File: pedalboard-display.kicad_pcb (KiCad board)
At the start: 2 copper layers, 24 x 24 mm, 32 parts, among them J1 02x02

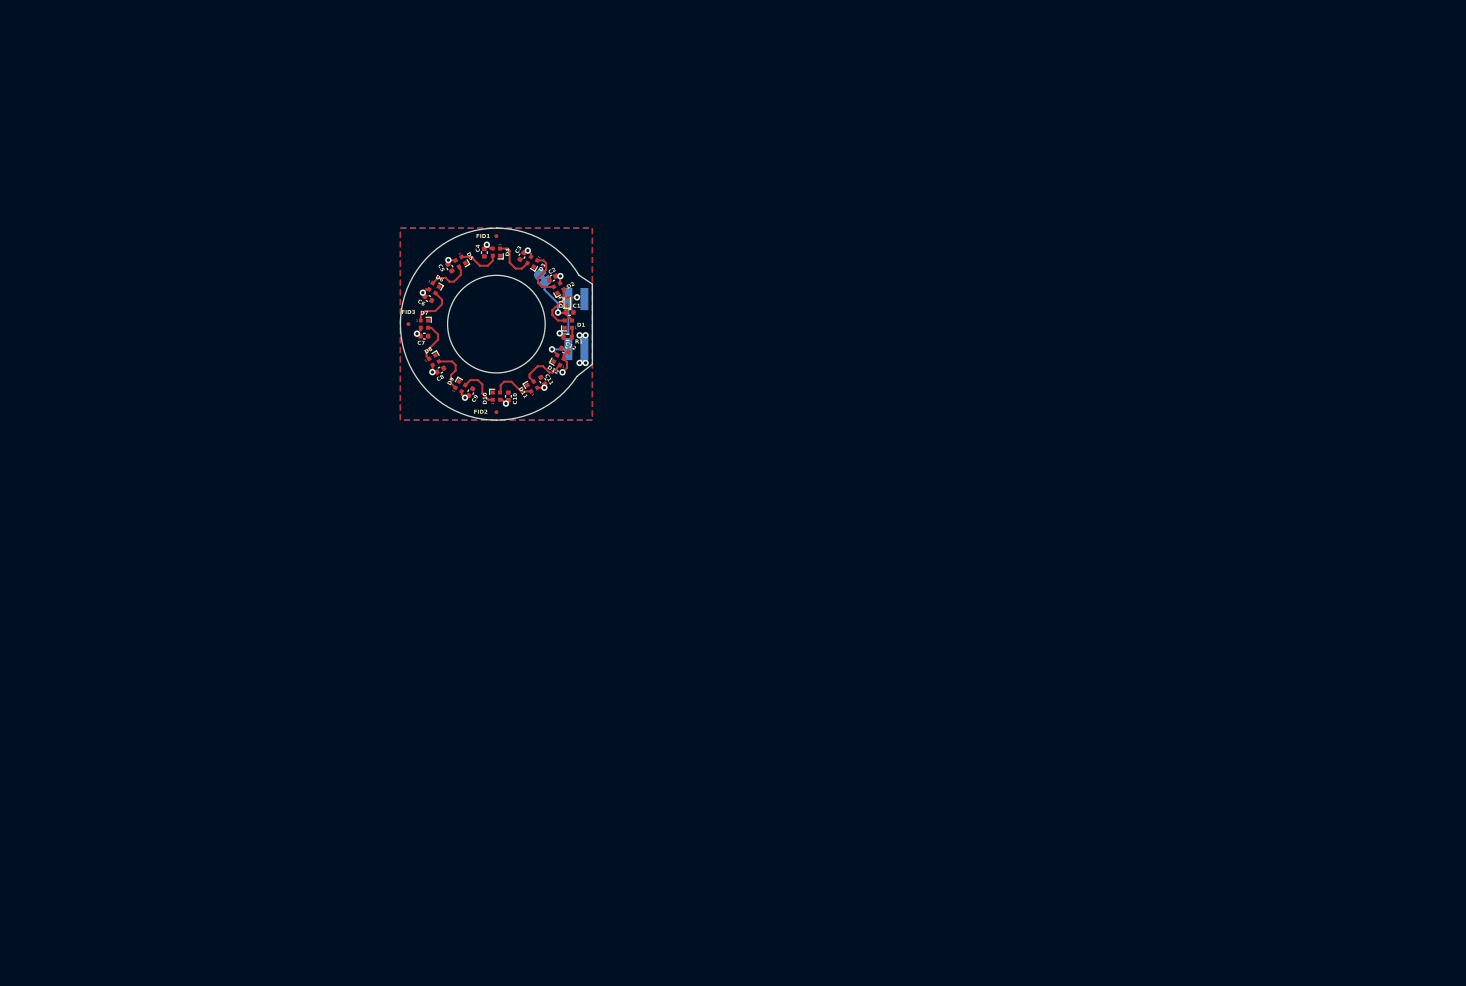
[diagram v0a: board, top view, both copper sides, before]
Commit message: First placement of parts on PCB
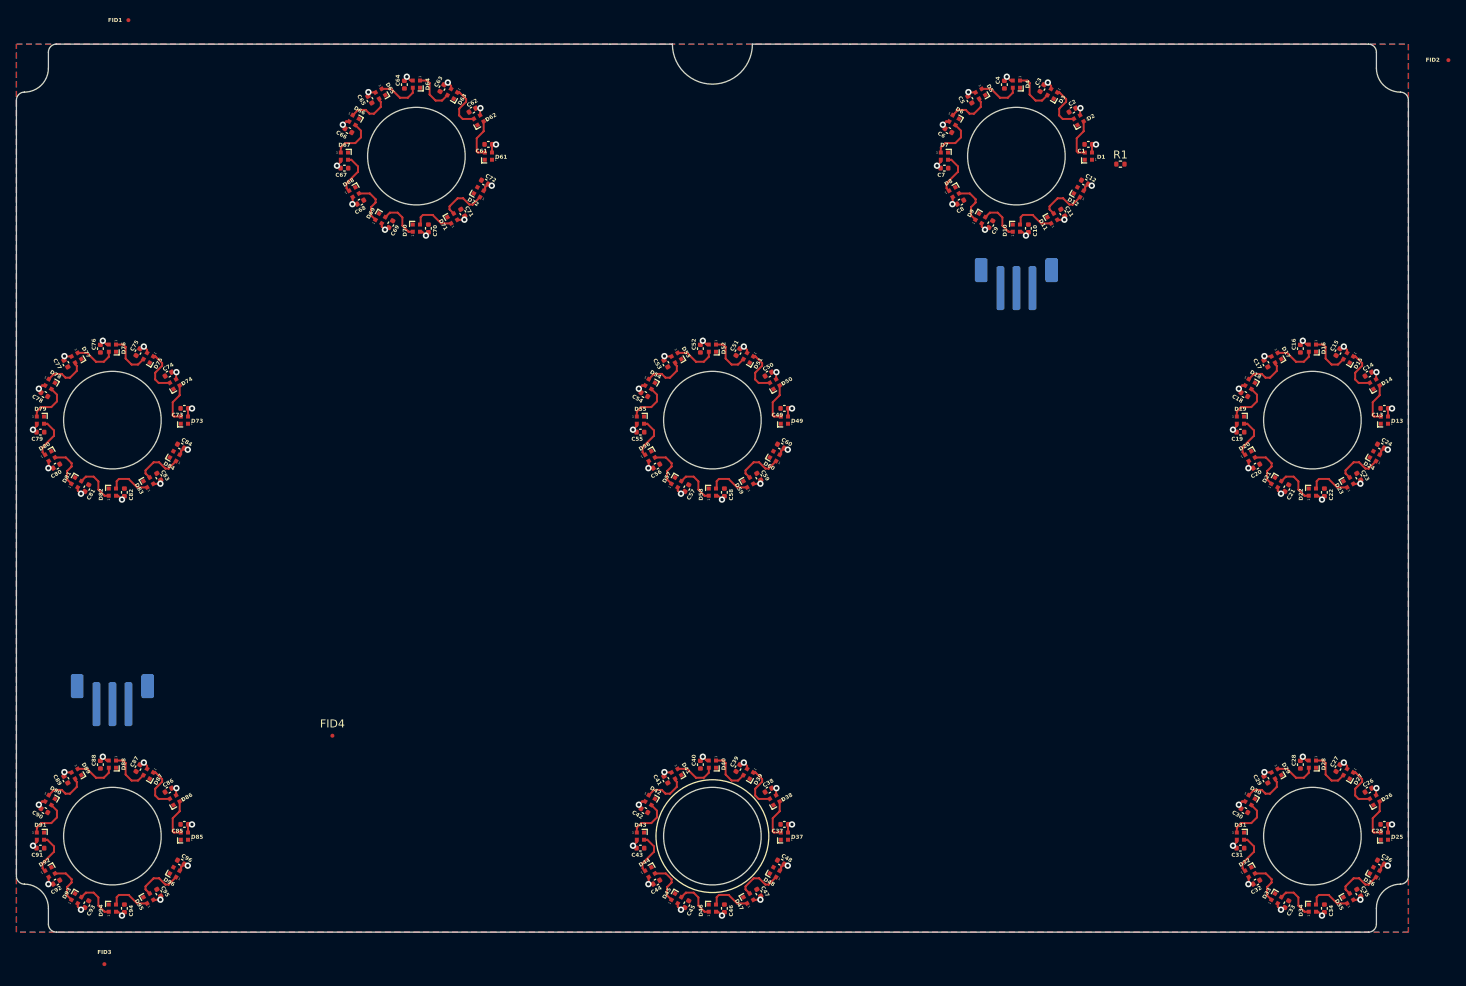
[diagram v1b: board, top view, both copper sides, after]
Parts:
- removed H4: Actuator Hole, Library:Actuator
- removed JP1: SJ, Jumper:SolderJumper-2_P1.3mm_Bridged_RoundedPad1.0x1.5mm
- added C13: 1uF, Capacitor_SMD:C_0402_1005Metric, F.Cu at (191.0, 70.5)
- added C14: 1uF, Capacitor_SMD:C_0402_1005Metric, F.Cu at (189.0, 66.2)
- added C15: 1uF, Capacitor_SMD:C_0402_1005Metric, F.Cu at (185.2, 63.5)
- added C16: 1uF, Capacitor_SMD:C_0402_1005Metric, F.Cu at (180.5, 63.1)
- added C17: 1uF, Capacitor_SMD:C_0402_1005Metric, F.Cu at (176.2, 64.9)
- added C18: 1uF, Capacitor_SMD:C_0402_1005Metric, F.Cu at (173.5, 68.8)
- added C19: 1uF, Capacitor_SMD:C_0402_1005Metric, F.Cu at (173.0, 73.5)
- added C20: 1uF, Capacitor_SMD:C_0402_1005Metric, F.Cu at (175.0, 77.8)
- added C21: 1uF, Capacitor_SMD:C_0402_1005Metric, F.Cu at (178.8, 80.5)
- added C22: 1uF, Capacitor_SMD:C_0402_1005Metric, F.Cu at (183.5, 81.0)
- added C23: 1uF, Capacitor_SMD:C_0402_1005Metric, F.Cu at (187.8, 79.1)
- added C24: 1uF, Capacitor_SMD:C_0402_1005Metric, F.Cu at (190.6, 75.2)
- added C25: 1uF, Capacitor_SMD:C_0402_1005Metric, F.Cu at (191.0, 122.5)
- added C26: 1uF, Capacitor_SMD:C_0402_1005Metric, F.Cu at (189.0, 118.2)
- added C27: 1uF, Capacitor_SMD:C_0402_1005Metric, F.Cu at (185.2, 115.5)
- added C28: 1uF, Capacitor_SMD:C_0402_1005Metric, F.Cu at (180.5, 115.1)
- added C29: 1uF, Capacitor_SMD:C_0402_1005Metric, F.Cu at (176.2, 116.9)
- added C30: 1uF, Capacitor_SMD:C_0402_1005Metric, F.Cu at (173.5, 120.8)
- added C31: 1uF, Capacitor_SMD:C_0402_1005Metric, F.Cu at (173.0, 125.5)
- added C32: 1uF, Capacitor_SMD:C_0402_1005Metric, F.Cu at (175.0, 129.8)
- added C33: 1uF, Capacitor_SMD:C_0402_1005Metric, F.Cu at (178.8, 132.5)
- added C34: 1uF, Capacitor_SMD:C_0402_1005Metric, F.Cu at (183.5, 133.0)
- added C35: 1uF, Capacitor_SMD:C_0402_1005Metric, F.Cu at (187.8, 131.1)
- added C36: 1uF, Capacitor_SMD:C_0402_1005Metric, F.Cu at (190.6, 127.2)
- added C37: 1uF, Capacitor_SMD:C_0402_1005Metric, F.Cu at (116.0, 122.5)
- added C38: 1uF, Capacitor_SMD:C_0402_1005Metric, F.Cu at (114.0, 118.2)
- added C39: 1uF, Capacitor_SMD:C_0402_1005Metric, F.Cu at (110.2, 115.5)
- added C40: 1uF, Capacitor_SMD:C_0402_1005Metric, F.Cu at (105.5, 115.1)
- added C41: 1uF, Capacitor_SMD:C_0402_1005Metric, F.Cu at (101.2, 116.9)
- added C42: 1uF, Capacitor_SMD:C_0402_1005Metric, F.Cu at (98.5, 120.8)
- added C43: 1uF, Capacitor_SMD:C_0402_1005Metric, F.Cu at (98.0, 125.5)
- added C44: 1uF, Capacitor_SMD:C_0402_1005Metric, F.Cu at (100.0, 129.8)
- added C45: 1uF, Capacitor_SMD:C_0402_1005Metric, F.Cu at (103.8, 132.5)
- added C46: 1uF, Capacitor_SMD:C_0402_1005Metric, F.Cu at (108.5, 133.0)
- added C47: 1uF, Capacitor_SMD:C_0402_1005Metric, F.Cu at (112.8, 131.1)
- added C48: 1uF, Capacitor_SMD:C_0402_1005Metric, F.Cu at (115.5, 127.2)
- added C49: 1uF, Capacitor_SMD:C_0402_1005Metric, F.Cu at (116.0, 70.5)
- added C50: 1uF, Capacitor_SMD:C_0402_1005Metric, F.Cu at (114.0, 66.2)
- added C51: 1uF, Capacitor_SMD:C_0402_1005Metric, F.Cu at (110.2, 63.5)
- added C52: 1uF, Capacitor_SMD:C_0402_1005Metric, F.Cu at (105.5, 63.1)
- added C53: 1uF, Capacitor_SMD:C_0402_1005Metric, F.Cu at (101.2, 64.9)
- added C54: 1uF, Capacitor_SMD:C_0402_1005Metric, F.Cu at (98.5, 68.8)
- added C55: 1uF, Capacitor_SMD:C_0402_1005Metric, F.Cu at (98.0, 73.5)
- added C56: 1uF, Capacitor_SMD:C_0402_1005Metric, F.Cu at (100.0, 77.8)
- added C57: 1uF, Capacitor_SMD:C_0402_1005Metric, F.Cu at (103.8, 80.5)
- added C58: 1uF, Capacitor_SMD:C_0402_1005Metric, F.Cu at (108.5, 81.0)
- added C59: 1uF, Capacitor_SMD:C_0402_1005Metric, F.Cu at (112.8, 79.1)
- added C60: 1uF, Capacitor_SMD:C_0402_1005Metric, F.Cu at (115.5, 75.2)
- added C61: 1uF, Capacitor_SMD:C_0402_1005Metric, F.Cu at (79.0, 37.5)
- added C62: 1uF, Capacitor_SMD:C_0402_1005Metric, F.Cu at (77.0, 33.2)
- added C63: 1uF, Capacitor_SMD:C_0402_1005Metric, F.Cu at (73.2, 30.5)
- added C64: 1uF, Capacitor_SMD:C_0402_1005Metric, F.Cu at (68.5, 30.1)
- added C65: 1uF, Capacitor_SMD:C_0402_1005Metric, F.Cu at (64.2, 31.9)
- added C66: 1uF, Capacitor_SMD:C_0402_1005Metric, F.Cu at (61.5, 35.8)
- added C67: 1uF, Capacitor_SMD:C_0402_1005Metric, F.Cu at (61.0, 40.5)
- added C68: 1uF, Capacitor_SMD:C_0402_1005Metric, F.Cu at (63.0, 44.8)
- added C69: 1uF, Capacitor_SMD:C_0402_1005Metric, F.Cu at (66.8, 47.5)
- added C70: 1uF, Capacitor_SMD:C_0402_1005Metric, F.Cu at (71.5, 48.0)
- added C71: 1uF, Capacitor_SMD:C_0402_1005Metric, F.Cu at (75.8, 46.1)
- added C72: 1uF, Capacitor_SMD:C_0402_1005Metric, F.Cu at (78.5, 42.2)
- added C73: 1uF, Capacitor_SMD:C_0402_1005Metric, F.Cu at (41.0, 70.5)
- added C74: 1uF, Capacitor_SMD:C_0402_1005Metric, F.Cu at (39.0, 66.2)
- added C75: 1uF, Capacitor_SMD:C_0402_1005Metric, F.Cu at (35.2, 63.5)
- added C76: 1uF, Capacitor_SMD:C_0402_1005Metric, F.Cu at (30.5, 63.1)
- added C77: 1uF, Capacitor_SMD:C_0402_1005Metric, F.Cu at (26.2, 64.9)
- added C78: 1uF, Capacitor_SMD:C_0402_1005Metric, F.Cu at (23.5, 68.8)
- added C79: 1uF, Capacitor_SMD:C_0402_1005Metric, F.Cu at (23.0, 73.5)
- added C80: 1uF, Capacitor_SMD:C_0402_1005Metric, F.Cu at (25.0, 77.8)
- added C81: 1uF, Capacitor_SMD:C_0402_1005Metric, F.Cu at (28.8, 80.5)
- added C82: 1uF, Capacitor_SMD:C_0402_1005Metric, F.Cu at (33.5, 81.0)
- added C83: 1uF, Capacitor_SMD:C_0402_1005Metric, F.Cu at (37.8, 79.1)
- added C84: 1uF, Capacitor_SMD:C_0402_1005Metric, F.Cu at (40.5, 75.2)
- added C85: 1uF, Capacitor_SMD:C_0402_1005Metric, F.Cu at (41.0, 122.5)
- added C86: 1uF, Capacitor_SMD:C_0402_1005Metric, F.Cu at (39.0, 118.2)
- added C87: 1uF, Capacitor_SMD:C_0402_1005Metric, F.Cu at (35.2, 115.5)
- added C88: 1uF, Capacitor_SMD:C_0402_1005Metric, F.Cu at (30.5, 115.1)
- added C89: 1uF, Capacitor_SMD:C_0402_1005Metric, F.Cu at (26.2, 116.9)
- added C90: 1uF, Capacitor_SMD:C_0402_1005Metric, F.Cu at (23.5, 120.8)
- added C91: 1uF, Capacitor_SMD:C_0402_1005Metric, F.Cu at (23.0, 125.5)
- added C92: 1uF, Capacitor_SMD:C_0402_1005Metric, F.Cu at (25.0, 129.8)
- added C93: 1uF, Capacitor_SMD:C_0402_1005Metric, F.Cu at (28.8, 132.5)
- added C94: 1uF, Capacitor_SMD:C_0402_1005Metric, F.Cu at (33.5, 133.0)
- added C95: 1uF, Capacitor_SMD:C_0402_1005Metric, F.Cu at (37.8, 131.1)
- added C96: 1uF, Capacitor_SMD:C_0402_1005Metric, F.Cu at (40.5, 127.2)
- added D14: SK6812_EC15, Library:LED_SK6812_EC15_1.5x1.5mm, F.Cu at (189.8, 67.5)
- added D15: SK6812_EC15, Library:LED_SK6812_EC15_1.5x1.5mm, F.Cu at (186.5, 64.2)
- added D16: SK6812_EC15, Library:LED_SK6812_EC15_1.5x1.5mm, F.Cu at (182.0, 63.0)
- added D17: SK6812_EC15, Library:LED_SK6812_EC15_1.5x1.5mm, F.Cu at (177.5, 64.2)
- added D18: SK6812_EC15, Library:LED_SK6812_EC15_1.5x1.5mm, F.Cu at (174.2, 67.5)
- added D19: SK6812_EC15, Library:LED_SK6812_EC15_1.5x1.5mm, F.Cu at (173.0, 72.0)
- added D20: SK6812_EC15, Library:LED_SK6812_EC15_1.5x1.5mm, F.Cu at (174.2, 76.5)
- added D21: SK6812_EC15, Library:LED_SK6812_EC15_1.5x1.5mm, F.Cu at (177.5, 79.8)
- added D22: SK6812_EC15, Library:LED_SK6812_EC15_1.5x1.5mm, F.Cu at (182.0, 81.0)
- added D23: SK6812_EC15, Library:LED_SK6812_EC15_1.5x1.5mm, F.Cu at (186.5, 79.8)
- added D24: SK6812_EC15, Library:LED_SK6812_EC15_1.5x1.5mm, F.Cu at (189.8, 76.5)
- added D25: SK6812_EC15, Library:LED_SK6812_EC15_1.5x1.5mm, F.Cu at (191.0, 124.0)
- added D26: SK6812_EC15, Library:LED_SK6812_EC15_1.5x1.5mm, F.Cu at (189.8, 119.5)
- added D27: SK6812_EC15, Library:LED_SK6812_EC15_1.5x1.5mm, F.Cu at (186.5, 116.2)
- added D28: SK6812_EC15, Library:LED_SK6812_EC15_1.5x1.5mm, F.Cu at (182.0, 115.0)
- added D29: SK6812_EC15, Library:LED_SK6812_EC15_1.5x1.5mm, F.Cu at (177.5, 116.2)
- added D30: SK6812_EC15, Library:LED_SK6812_EC15_1.5x1.5mm, F.Cu at (174.2, 119.5)
- added D31: SK6812_EC15, Library:LED_SK6812_EC15_1.5x1.5mm, F.Cu at (173.0, 124.0)
- added D32: SK6812_EC15, Library:LED_SK6812_EC15_1.5x1.5mm, F.Cu at (174.2, 128.5)
- added D33: SK6812_EC15, Library:LED_SK6812_EC15_1.5x1.5mm, F.Cu at (177.5, 131.8)
- added D34: SK6812_EC15, Library:LED_SK6812_EC15_1.5x1.5mm, F.Cu at (182.0, 133.0)
- added D35: SK6812_EC15, Library:LED_SK6812_EC15_1.5x1.5mm, F.Cu at (186.5, 131.8)
- added D36: SK6812_EC15, Library:LED_SK6812_EC15_1.5x1.5mm, F.Cu at (189.8, 128.5)
- added D37: SK6812_EC15, Library:LED_SK6812_EC15_1.5x1.5mm, F.Cu at (116.0, 124.0)
- added D38: SK6812_EC15, Library:LED_SK6812_EC15_1.5x1.5mm, F.Cu at (114.8, 119.5)
- added D39: SK6812_EC15, Library:LED_SK6812_EC15_1.5x1.5mm, F.Cu at (111.5, 116.2)
- added D40: SK6812_EC15, Library:LED_SK6812_EC15_1.5x1.5mm, F.Cu at (107.0, 115.0)
- added D41: SK6812_EC15, Library:LED_SK6812_EC15_1.5x1.5mm, F.Cu at (102.5, 116.2)
- added D42: SK6812_EC15, Library:LED_SK6812_EC15_1.5x1.5mm, F.Cu at (99.2, 119.5)
- added D43: SK6812_EC15, Library:LED_SK6812_EC15_1.5x1.5mm, F.Cu at (98.0, 124.0)
- added D44: SK6812_EC15, Library:LED_SK6812_EC15_1.5x1.5mm, F.Cu at (99.2, 128.5)
- added D45: SK6812_EC15, Library:LED_SK6812_EC15_1.5x1.5mm, F.Cu at (102.5, 131.8)
- added D46: SK6812_EC15, Library:LED_SK6812_EC15_1.5x1.5mm, F.Cu at (107.0, 133.0)
- added D47: SK6812_EC15, Library:LED_SK6812_EC15_1.5x1.5mm, F.Cu at (111.5, 131.8)
- added D48: SK6812_EC15, Library:LED_SK6812_EC15_1.5x1.5mm, F.Cu at (114.8, 128.5)
- added D49: SK6812_EC15, Library:LED_SK6812_EC15_1.5x1.5mm, F.Cu at (116.0, 72.0)
- added D50: SK6812_EC15, Library:LED_SK6812_EC15_1.5x1.5mm, F.Cu at (114.8, 67.5)
- added D51: SK6812_EC15, Library:LED_SK6812_EC15_1.5x1.5mm, F.Cu at (111.5, 64.2)
- added D52: SK6812_EC15, Library:LED_SK6812_EC15_1.5x1.5mm, F.Cu at (107.0, 63.0)
- added D53: SK6812_EC15, Library:LED_SK6812_EC15_1.5x1.5mm, F.Cu at (102.5, 64.2)
- added D54: SK6812_EC15, Library:LED_SK6812_EC15_1.5x1.5mm, F.Cu at (99.2, 67.5)
- added D55: SK6812_EC15, Library:LED_SK6812_EC15_1.5x1.5mm, F.Cu at (98.0, 72.0)
- added D56: SK6812_EC15, Library:LED_SK6812_EC15_1.5x1.5mm, F.Cu at (99.2, 76.5)
- added D57: SK6812_EC15, Library:LED_SK6812_EC15_1.5x1.5mm, F.Cu at (102.5, 79.8)
- added D58: SK6812_EC15, Library:LED_SK6812_EC15_1.5x1.5mm, F.Cu at (107.0, 81.0)
- added D59: SK6812_EC15, Library:LED_SK6812_EC15_1.5x1.5mm, F.Cu at (111.5, 79.8)
- added D60: SK6812_EC15, Library:LED_SK6812_EC15_1.5x1.5mm, F.Cu at (114.8, 76.5)
- added D61: SK6812_EC15, Library:LED_SK6812_EC15_1.5x1.5mm, F.Cu at (79.0, 39.0)
- added D62: SK6812_EC15, Library:LED_SK6812_EC15_1.5x1.5mm, F.Cu at (77.8, 34.5)
- added D63: SK6812_EC15, Library:LED_SK6812_EC15_1.5x1.5mm, F.Cu at (74.5, 31.2)
- added D64: SK6812_EC15, Library:LED_SK6812_EC15_1.5x1.5mm, F.Cu at (70.0, 30.0)
- added D65: SK6812_EC15, Library:LED_SK6812_EC15_1.5x1.5mm, F.Cu at (65.5, 31.2)
- added D66: SK6812_EC15, Library:LED_SK6812_EC15_1.5x1.5mm, F.Cu at (62.2, 34.5)
- added D67: SK6812_EC15, Library:LED_SK6812_EC15_1.5x1.5mm, F.Cu at (61.0, 39.0)
- added D68: SK6812_EC15, Library:LED_SK6812_EC15_1.5x1.5mm, F.Cu at (62.2, 43.5)
- added D69: SK6812_EC15, Library:LED_SK6812_EC15_1.5x1.5mm, F.Cu at (65.5, 46.8)
- added D70: SK6812_EC15, Library:LED_SK6812_EC15_1.5x1.5mm, F.Cu at (70.0, 48.0)
- added D71: SK6812_EC15, Library:LED_SK6812_EC15_1.5x1.5mm, F.Cu at (74.5, 46.8)
- added D72: SK6812_EC15, Library:LED_SK6812_EC15_1.5x1.5mm, F.Cu at (77.8, 43.5)
- added D73: SK6812_EC15, Library:LED_SK6812_EC15_1.5x1.5mm, F.Cu at (41.0, 72.0)
- added D74: SK6812_EC15, Library:LED_SK6812_EC15_1.5x1.5mm, F.Cu at (39.8, 67.5)
- added D75: SK6812_EC15, Library:LED_SK6812_EC15_1.5x1.5mm, F.Cu at (36.5, 64.2)
- added D76: SK6812_EC15, Library:LED_SK6812_EC15_1.5x1.5mm, F.Cu at (32.0, 63.0)
- added D77: SK6812_EC15, Library:LED_SK6812_EC15_1.5x1.5mm, F.Cu at (27.5, 64.2)
- added D78: SK6812_EC15, Library:LED_SK6812_EC15_1.5x1.5mm, F.Cu at (24.2, 67.5)
- added D79: SK6812_EC15, Library:LED_SK6812_EC15_1.5x1.5mm, F.Cu at (23.0, 72.0)
- added D80: SK6812_EC15, Library:LED_SK6812_EC15_1.5x1.5mm, F.Cu at (24.2, 76.5)
- added D81: SK6812_EC15, Library:LED_SK6812_EC15_1.5x1.5mm, F.Cu at (27.5, 79.8)
- added D82: SK6812_EC15, Library:LED_SK6812_EC15_1.5x1.5mm, F.Cu at (32.0, 81.0)
- added D83: SK6812_EC15, Library:LED_SK6812_EC15_1.5x1.5mm, F.Cu at (36.5, 79.8)
- added D84: SK6812_EC15, Library:LED_SK6812_EC15_1.5x1.5mm, F.Cu at (39.8, 76.5)
- added D85: SK6812_EC15, Library:LED_SK6812_EC15_1.5x1.5mm, F.Cu at (41.0, 124.0)
- added D86: SK6812_EC15, Library:LED_SK6812_EC15_1.5x1.5mm, F.Cu at (39.8, 119.5)
- added D87: SK6812_EC15, Library:LED_SK6812_EC15_1.5x1.5mm, F.Cu at (36.5, 116.2)
- added D88: SK6812_EC15, Library:LED_SK6812_EC15_1.5x1.5mm, F.Cu at (32.0, 115.0)
- added D89: SK6812_EC15, Library:LED_SK6812_EC15_1.5x1.5mm, F.Cu at (27.5, 116.2)
- added D90: SK6812_EC15, Library:LED_SK6812_EC15_1.5x1.5mm, F.Cu at (24.2, 119.5)
- added D91: SK6812_EC15, Library:LED_SK6812_EC15_1.5x1.5mm, F.Cu at (23.0, 124.0)
- added D92: SK6812_EC15, Library:LED_SK6812_EC15_1.5x1.5mm, F.Cu at (24.2, 128.5)
- added D93: SK6812_EC15, Library:LED_SK6812_EC15_1.5x1.5mm, F.Cu at (27.5, 131.8)
- added D94: SK6812_EC15, Library:LED_SK6812_EC15_1.5x1.5mm, F.Cu at (32.0, 133.0)
- added D95: SK6812_EC15, Library:LED_SK6812_EC15_1.5x1.5mm, F.Cu at (36.5, 131.8)
- added D96: SK6812_EC15, Library:LED_SK6812_EC15_1.5x1.5mm, F.Cu at (39.8, 128.5)
- added FID4: Fiducial, Fiducial:Fiducial_0.5mm_Mask1mm, F.Cu at (59.5, 111.5)
- added J2: Conn_01x03_Pin, Connector_JST:JST_PH_B3B-PH-SM4-TB_1x03-1MP_P2.00mm_Vertical, B.Cu at (32.0, 107.0)
- D13: value 1N4148W -> SK6812_EC15; footprint Diode_SMD:D_SOD-923 -> Library:LED_SK6812_EC15_1.5x1.5mm
- J1: value 02x02 -> Conn_01x03_Pin; footprint Connector_PinSocket_2.00mm:PinSocket_2x02_P2.00mm_Vertical_SMD -> Connector_JST:JST_PH_B3B-PH-SM4-TB_1x03-1MP_P2.00mm_Vertical
- moved FID2 126.9 mm to (199.0, 27.0)
- moved D13 103.2 mm to (191.0, 72.0), turned to 180 degrees
- moved FID3 88.6 mm to (31.0, 140.0)
- moved R1 72.4 mm to (158.0, 40.0), turned to 0 degrees
- moved C11 68.3 mm to (150.8, 46.1)
- moved C12 68.3 mm to (153.6, 42.2)
- moved C9 68.3 mm to (141.8, 47.5)
- moved C10 68.3 mm to (146.5, 48.0)
- moved C2 68.3 mm to (152.0, 33.2)
- moved C4 68.3 mm to (143.5, 30.1)
- moved C5 68.3 mm to (139.2, 31.9)
- moved C6 68.3 mm to (136.5, 35.8)
- moved C7 68.3 mm to (136.0, 40.5)
- moved C8 68.3 mm to (138.0, 44.8)
- moved D1 68.3 mm to (154.0, 39.0)
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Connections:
- C1 pad 1: Net-(D1-VDD) -> VCC
- D1 pad 1: Net-(D1-DIN) -> /Led Ring GAIN/D_IN
- D1 pad 2: Net-(D1-VDD) -> VCC
- D12 pad 3: Net-(D12-DOUT) -> /Led Ring F/D_IN
- D13 pad 1: Net-(D1-VDD) -> /Led Ring F/D_IN
- J1 pad 1: VCC -> GND
- J1 pad 2: GND -> VCC
- R1 pad 1: Net-(D1-DIN) -> Net-(J1-Pin_3)
- R1 pad 2: Net-(J1-Pin_3) -> /Led Ring GAIN/D_IN
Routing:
- net VCC: track 13.9 -> 95.1 mm, vias 12 -> 96
- net Net-(D1-VDD): track 7.63 -> 0.00 mm, vias 1 -> 0
- net Net-(J1-Pin_3): track 6.09 -> 0.00 mm, vias 1 -> 0
- net Net-(D35-DOUT): track 0.00 -> 6.08 mm
- net Net-(D23-DOUT): track 0.00 -> 6.08 mm
- net Net-(D95-DOUT): track 0.00 -> 6.08 mm
- net Net-(D83-DOUT): track 0.00 -> 6.08 mm
- net Net-(D47-DOUT): track 0.00 -> 6.08 mm
- net Net-(D59-DOUT): track 0.00 -> 6.08 mm
- net Net-(D71-DOUT): track 0.00 -> 6.08 mm
- net GND: track 5.97 -> 0.00 mm, vias 4 -> 0
- net Net-(D26-DOUT): track 0.00 -> 5.85 mm
- net Net-(D62-DOUT): track 0.00 -> 5.85 mm
- net Net-(D14-DOUT): track 0.00 -> 5.85 mm
- net Net-(D50-DOUT): track 0.00 -> 5.85 mm
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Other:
- board size 24 x 24 mm -> 174 x 111 mm
- board text added: "${TITLE} ${COMPANY} PCB: v${REVISION} ($:${GIT_HASH})"
- board text removed: "${COMPANY}"
- board text removed: "${TITLE}"
- board text removed: "D0"
- board text removed: "DI"
- board text removed: "GND"
- board text removed: "PCB: v${REVISION} $:${GIT_HASH}"
- board text removed: "VCC"

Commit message: Connectedx all LEDs
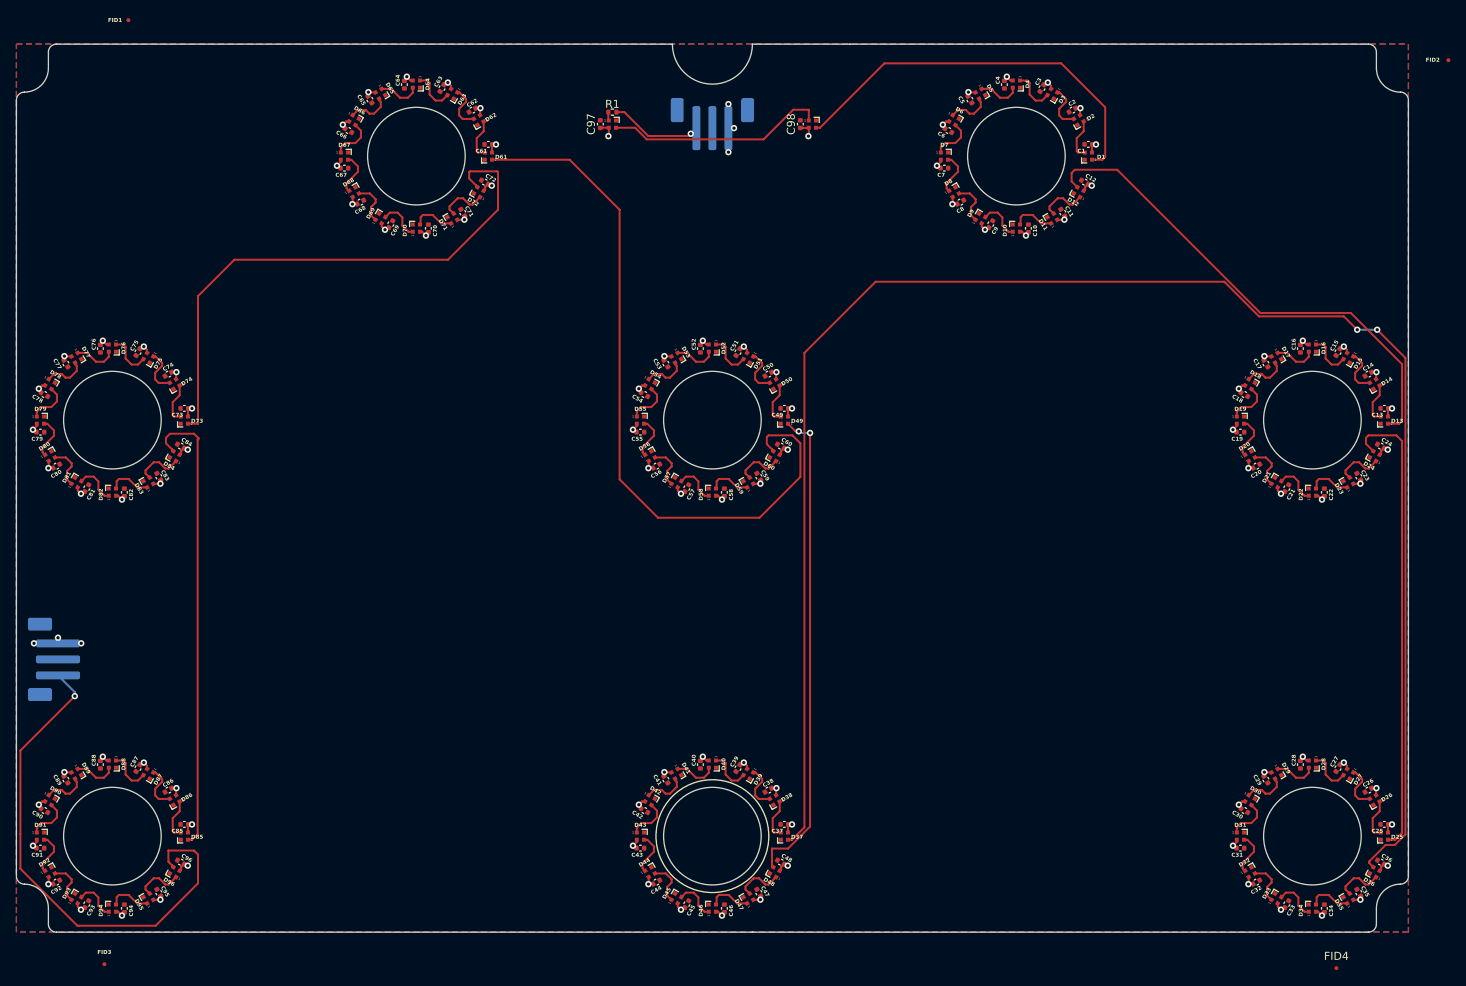
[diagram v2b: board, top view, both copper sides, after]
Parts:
- added C97: 1uF, Capacitor_SMD:C_0402_1005Metric, F.Cu at (93.0, 35.0)
- added C98: 1uF, Capacitor_SMD:C_0402_1005Metric, F.Cu at (118.0, 35.0)
- added D97: SK6812_EC15, Library:LED_SK6812_EC15_1.5x1.5mm, F.Cu at (94.5, 35.0)
- added D98: SK6812_EC15, Library:LED_SK6812_EC15_1.5x1.5mm, F.Cu at (119.5, 35.0)
- moved FID4 128.8 mm to (185.0, 140.5)
- moved R1 63.8 mm to (94.5, 33.5), turned to 180 degrees
- moved J1 42.9 mm to (107.0, 35.0)
- moved J2 8.91 mm to (24.7, 101.9), turned to -90 degrees
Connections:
- R1 pad 2: /Led Ring GAIN/D_IN -> Net-(D97-DIN)
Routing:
- net /Led Ring B/D_IN: track 0.06 -> 211.2 mm, vias 0 -> 2
- net /Led Ring E/D_OUT: track 0.06 -> 90.0 mm
- net /Led Ring D/D_IN: track 0.06 -> 69.9 mm
- net /Led Ring A/D_OUT: track 0.06 -> 65.1 mm, vias 0 -> 1
- net /Led Ring F/D_IN: track 0.06 -> 62.7 mm
- net /Led Ring B/D_OUT: track 0.06 -> 60.8 mm, vias 0 -> 2
- net /Led Ring C/D_IN: track 0.06 -> 58.1 mm
- net /Led Ring A/D_IN: track 0.06 -> 57.7 mm
- net /Led Ring GAIN/D_IN: track 0.00 -> 49.8 mm
- net Net-(D97-DOUT): track 0.00 -> 27.6 mm
- net GND: track 0.00 -> 13.3 mm, vias 0 -> 6
- net Net-(J1-Pin_3): track 0.00 -> 11.6 mm, vias 0 -> 1
- net VCC: track 95.1 -> 99.3 mm, vias 96 -> 98
- net Net-(D97-DIN): track 0.00 -> 1.07 mm

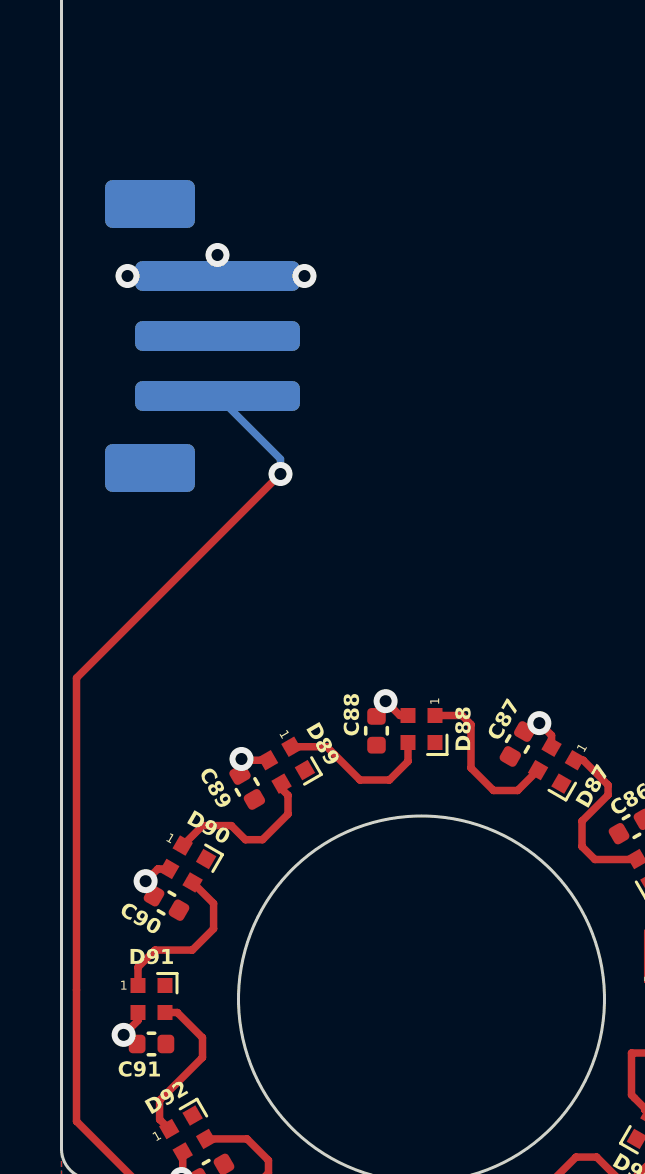
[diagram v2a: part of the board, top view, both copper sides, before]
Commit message: Improve user drawings
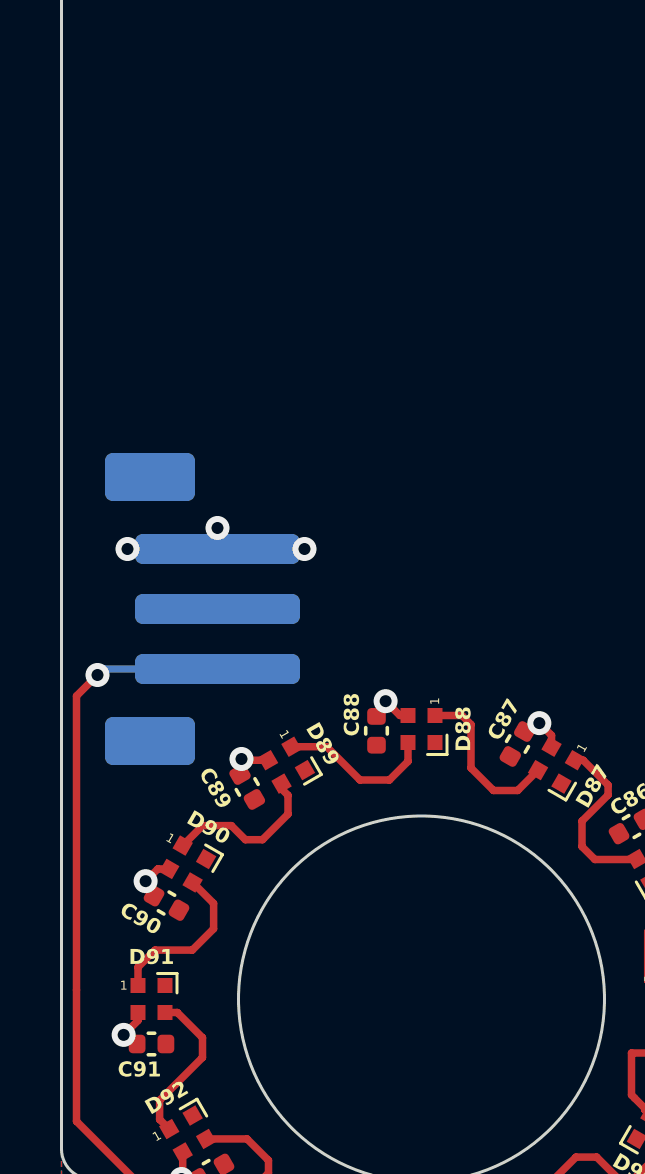
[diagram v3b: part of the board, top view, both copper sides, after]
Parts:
- moved J2 9.10 mm to (24.7, 111.0)
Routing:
- net /Led Ring A/D_OUT: track 65.1 -> 56.5 mm
